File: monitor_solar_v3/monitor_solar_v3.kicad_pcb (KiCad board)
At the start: 2 copper layers, 100 x 50 mm, 42 parts, among them J1 Panel, J10 GPIO, J11 Jumper, J2 ACS712, J3 Battery, J4 AMP_OUT, J5 JUMPER_PROG, J6 JUMPER_PROG, J7 PROGRAM, J9 Reg 5V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

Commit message: PCB V3 finished
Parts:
- added R15: 10k, Resistor_THT:R_Axial_DIN0207_L6.3mm_D2.5mm_P10.16mm_Horizontal, F.Cu at (48.4, 30.8)
- moved J5 2.06 mm to (43.9, 41.0)
- moved R2 1.60 mm to (39.1, 48.2)
- moved G*** 1.17 mm to (30.1, 32.8)
- moved C2 0.65 mm to (84.0, 47.2)
- moved J6 0.15 mm to (41.3, 34.4)
- moved C5 0.10 mm to (105.1, 45.1)
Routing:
- net GND: track 351.8 -> 344.7 mm
- net GPIO2: track 7.04 -> 9.17 mm
- net GPIO15: track 6.98 -> 8.98 mm
- net +5V: track 113.0 -> 111.7 mm
- net Net-(U4A-+): track 15.7 -> 15.0 mm
- added copper zone on B.Cu, net GND
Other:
- board text added: "Monitor Solar Pablo G. 2025"

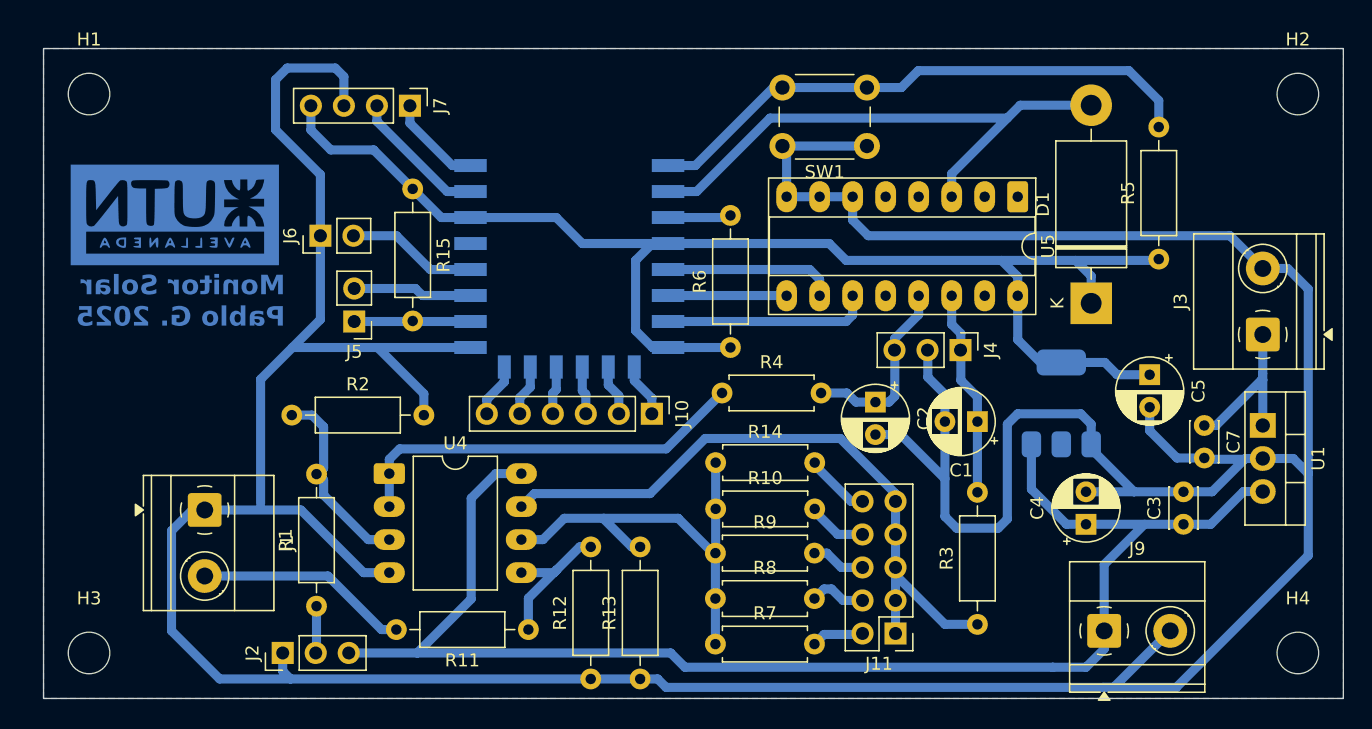
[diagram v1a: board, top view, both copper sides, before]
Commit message: Add led for power status
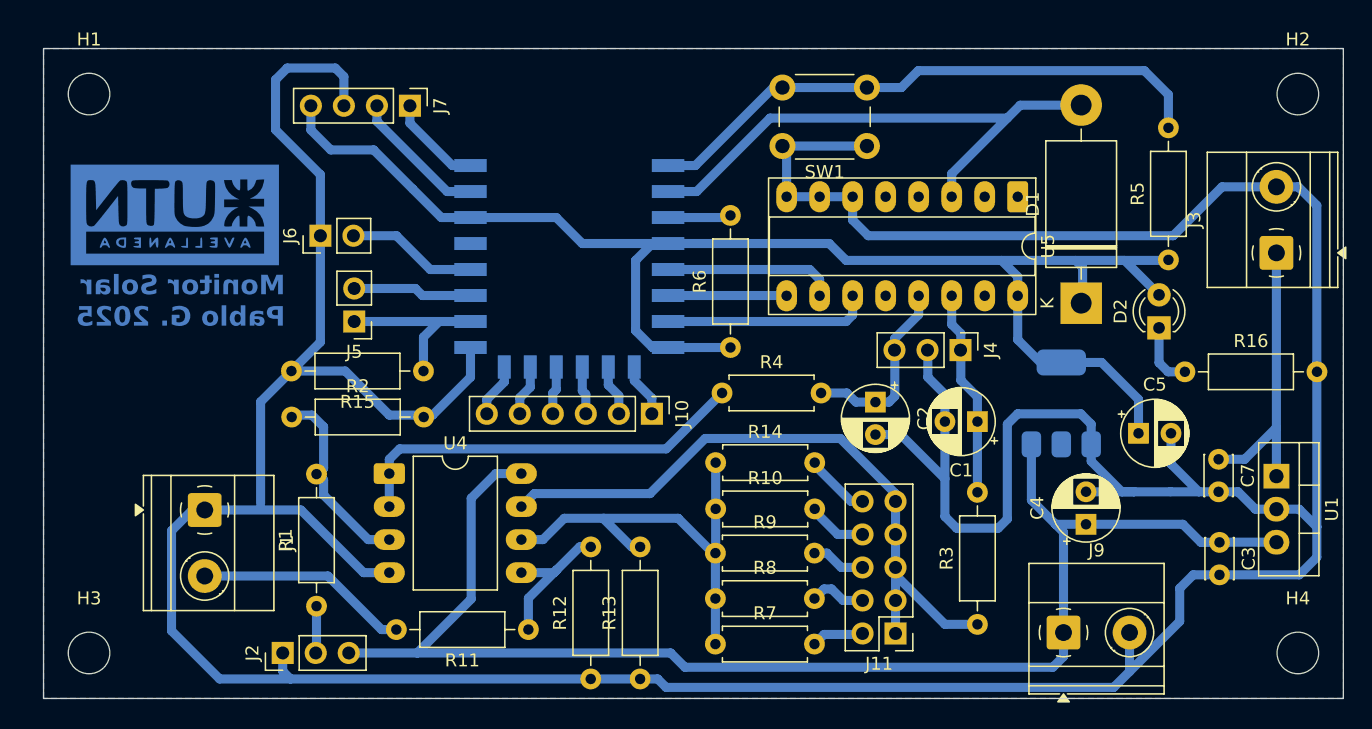
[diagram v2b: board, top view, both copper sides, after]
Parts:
- added D2: LED G, LED_THT:LED_D3.0mm, F.Cu at (105.8, 41.5)
- added R16: 470, Resistor_THT:R_Axial_DIN0207_L6.3mm_D2.5mm_P10.16mm_Horizontal, F.Cu at (107.8, 44.9)
- moved R15 14.0 mm to (49.2, 44.8), turned to 180 degrees
- moved J3 6.37 mm to (114.8, 35.7)
- moved C5 4.59 mm to (104.2, 49.6), turned to 0 degrees
- moved U1 4.04 mm to (114.8, 52.9)
- moved J9 3.13 mm to (98.5, 64.9)
- moved C3 3.10 mm to (110.5, 58.0), turned to -90 degrees
- moved C7 2.82 mm to (110.4, 51.6)
- moved D1 0.77 mm to (99.8, 39.6)
- moved R5 0.74 mm to (106.5, 36.3)
- moved R2 0.15 mm to (39.1, 48.4)
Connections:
- R15 pad 1: +3.3V -> GPIO15
- R15 pad 2: GPIO15 -> GND
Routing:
- net +BATT: track 12.9 -> 22.9 mm
- net +3.3V: track 109.3 -> 116.7 mm
- net Net-(D2-K): track 0.00 -> 4.96 mm
- net GPIO15: track 8.98 -> 13.3 mm
- net +5V: track 111.7 -> 109.0 mm
- net Net-(U3-~{RST}): track 43.8 -> 44.8 mm
- net ADC_IN: track 43.1 -> 42.4 mm
